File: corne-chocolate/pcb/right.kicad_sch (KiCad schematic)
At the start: 79 parts, among them J3 MJ-4PP-9, J4 Conn_01x04, P3 Conn_01x01, P4 Conn_01x01, SW13 SW_PUSH, SW22 SW_PUSH, SW23 SW_PUSH, SW24 SW_PUSH, SW25 SW_PUSH, SW26 SW_PUSH, SW27 SW_PUSH, SW28 SW_PUSH, SW29 SW_PUSH, SW30 SW_PUSH, SW31 SW_PUSH, SW32 SW_PUSH, SW33 SW_PUSH, SW34 SW_PUSH, SW35 SW_PUSH, SW36 SW_PUSH, SW37 SW_PUSH, SW7 SW_PUSH, U2 ProMicro

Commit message: several important fixes
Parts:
- removed J3: MJ-4PP-9, kbd:MJ-4PP-9_1side, symbol kbd:MJ-4PP-9
- removed J4: Conn_01x04, kbd:OLED_1side, symbol Connector_Generic:Conn_01x04
- removed JP6, JP7, JP8, JP9: Device:Jumper_NO_Small, kbd:Jumper, symbol kbd:Jumper_NO_Small-Device
- removed L13, L30, L31, L32, L33, L36, L37, L38, L39, L40, L41, L42, L43, L46, L47, L48, L49, L7: SK6812MINI, kbd:YS-SK6812MINI-E, symbol kbd:SK6812MINI
- removed L28, L29, L34, L35, L44, L45: SK6812MINI, kbd:SK6812MINI_underglow_rev, symbol kbd:SK6812MINI
- removed P3: Conn_01x01, kbd:1pin_conn, symbol Connector_Generic:Conn_01x01
- removed R3, R4: R, kbd:R, symbol Device:R
- added J3: 781271220, kbd:CON_781271220, symbol kbd:781271220
- added J4: 54-00174, kbd:54-00174_TEN, symbol kbd:54-00174
- added LED25, LED26, LED27, LED28, LED29, LED31, LED32, LED34, LED35, LED37, LED38, LED39, LED40, LED41, LED43, LED44, LED46, LED47: YS-SK6812MINI-E, kbd:LED_SK6812-MINI-E, symbol kbd:LED_SK6812MINI-E
- added LED30, LED33, LED36, LED42, LED45, LED48: WS2812B, kbd:LED_WS2812B_PLCC4_5.0x5.0mm_P3.2mm, symbol kbd:WS2812B
- added R3, R4: 4k7, kbd:R_1206_3216Metric_Pad1.30x1.75mm_HandSolder, symbol kbd:R
- D19: renamed from D7; item qty 100 -> (none); supplier Amazon -> Digikey; supplier pn B09DR5KFXM -> 1655-1N4148WCT-ND; vendor site https://www.amazon.com/Adafruit-Industries-1N4148-SOD-123-D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 -> (none)
- D20: renamed from D23; item qty 100 -> (none); supplier Amazon -> Digikey; supplier pn B09DR5KFXM -> 1655-1N4148WCT-ND; vendor site https://www.amazon.com/Adafruit-Industries-1N4148-SOD-123-D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 -> (none)
- D21: renamed from D26; item qty 100 -> (none); supplier Amazon -> Digikey; supplier pn B09DR5KFXM -> 1655-1N4148WCT-ND; vendor site https://www.amazon.com/Adafruit-Industries-1N4148-SOD-123-D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 -> (none)
- D22: renamed from D30; item qty 100 -> (none); supplier Amazon -> Digikey; supplier pn B09DR5KFXM -> 1655-1N4148WCT-ND; vendor site https://www.amazon.com/Adafruit-Industries-1N4148-SOD-123-D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 -> (none)
- D23: renamed from D34; item qty 100 -> (none); supplier Amazon -> Digikey; supplier pn B09DR5KFXM -> 1655-1N4148WCT-ND; vendor site https://www.amazon.com/Adafruit-Industries-1N4148-SOD-123-D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 -> (none)
- D24: renamed from D13; item qty 100 -> (none); supplier Amazon -> Digikey; supplier pn B09DR5KFXM -> 1655-1N4148WCT-ND; vendor site https://www.amazon.com/Adafruit-Industries-1N4148-SOD-123-D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 -> (none)
- D25: renamed from D24; item qty 100 -> (none); supplier Amazon -> Digikey; supplier pn B09DR5KFXM -> 1655-1N4148WCT-ND; vendor site https://www.amazon.com/Adafruit-Industries-1N4148-SOD-123-D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 -> (none)
- D26: renamed from D27; item qty 100 -> (none); supplier Amazon -> Digikey; supplier pn B09DR5KFXM -> 1655-1N4148WCT-ND; vendor site https://www.amazon.com/Adafruit-Industries-1N4148-SOD-123-D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 -> (none)
- D27: renamed from D31; item qty 100 -> (none); supplier Amazon -> Digikey; supplier pn B09DR5KFXM -> 1655-1N4148WCT-ND; vendor site https://www.amazon.com/Adafruit-Industries-1N4148-SOD-123-D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 -> (none)
- D28: renamed from D35; item qty 100 -> (none); supplier Amazon -> Digikey; supplier pn B09DR5KFXM -> 1655-1N4148WCT-ND; vendor site https://www.amazon.com/Adafruit-Industries-1N4148-SOD-123-D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 -> (none)
- D29: renamed from D22; item qty 100 -> (none); supplier Amazon -> Digikey; supplier pn B09DR5KFXM -> 1655-1N4148WCT-ND; vendor site https://www.amazon.com/Adafruit-Industries-1N4148-SOD-123-D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 -> (none)
- D30: renamed from D25; item qty 100 -> (none); supplier Amazon -> Digikey; supplier pn B09DR5KFXM -> 1655-1N4148WCT-ND; vendor site https://www.amazon.com/Adafruit-Industries-1N4148-SOD-123-D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 -> (none)
- D31: renamed from D28; item qty 100 -> (none); supplier Amazon -> Digikey; supplier pn B09DR5KFXM -> 1655-1N4148WCT-ND; vendor site https://www.amazon.com/Adafruit-Industries-1N4148-SOD-123-D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 -> (none)
- D32: item qty 100 -> (none); supplier Amazon -> Digikey; supplier pn B09DR5KFXM -> 1655-1N4148WCT-ND; vendor site https://www.amazon.com/Adafruit-Industries-1N4148-SOD-123-D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 -> (none)
- D33: renamed from D36; item qty 100 -> (none); supplier Amazon -> Digikey; supplier pn B09DR5KFXM -> 1655-1N4148WCT-ND; vendor site https://www.amazon.com/Adafruit-Industries-1N4148-SOD-123-D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 -> (none)
- D34: renamed from D29; item qty 100 -> (none); supplier Amazon -> Digikey; supplier pn B09DR5KFXM -> 1655-1N4148WCT-ND; vendor site https://www.amazon.com/Adafruit-Industries-1N4148-SOD-123-D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 -> (none)
- D35: renamed from D33; item qty 100 -> (none); supplier Amazon -> Digikey; supplier pn B09DR5KFXM -> 1655-1N4148WCT-ND; vendor site https://www.amazon.com/Adafruit-Industries-1N4148-SOD-123-D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 -> (none)
- D36: renamed from D37; item qty 100 -> (none); supplier Amazon -> Digikey; supplier pn B09DR5KFXM -> 1655-1N4148WCT-ND; vendor site https://www.amazon.com/Adafruit-Industries-1N4148-SOD-123-D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 -> (none)
- RSW2: item qty 50 -> (none); supplier Amazon -> Digikey; supplier 2 pn (none) -> B07H9ZSZD4; supplier pn B07H9ZSZD4 -> CKN12301-ND; supplier2 (none) -> Amazon; vendor site https://www.amazon.com/-/es/uxcell-0-118x0-236x0-197-Peque%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 -> (none)
- SW19: renamed from SW7; item qty 100 -> (none); supplier Amazon -> Digikey; supplier 2 pn (none) -> B0CPVJLMDJ; supplier pn B0CPVJLMDJ -> 1528-5118-ND; supplier2 (none) -> Amazon; vendor site https://www.amazon.com/100Pieces-Chocolate-Switches-Accesso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 -> (none)
- SW20: renamed from SW23; item qty 100 -> (none); supplier Amazon -> Digikey; supplier 2 pn (none) -> B0CPVJLMDJ; supplier pn B0CPVJLMDJ -> 1528-5118-ND; supplier2 (none) -> Amazon; vendor site https://www.amazon.com/100Pieces-Chocolate-Switches-Accesso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 -> (none)
- SW21: renamed from SW26; item qty 100 -> (none); supplier Amazon -> Digikey; supplier 2 pn (none) -> B0CPVJLMDJ; supplier pn B0CPVJLMDJ -> 1528-5118-ND; supplier2 (none) -> Amazon; vendor site https://www.amazon.com/100Pieces-Chocolate-Switches-Accesso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 -> (none)
- SW22: renamed from SW30; item qty 100 -> (none); supplier Amazon -> Digikey; supplier 2 pn (none) -> B0CPVJLMDJ; supplier pn B0CPVJLMDJ -> 1528-5118-ND; supplier2 (none) -> Amazon; vendor site https://www.amazon.com/100Pieces-Chocolate-Switches-Accesso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 -> (none)
- SW23: renamed from SW34; item qty 100 -> (none); supplier Amazon -> Digikey; supplier 2 pn (none) -> B0CPVJLMDJ; supplier pn B0CPVJLMDJ -> 1528-5118-ND; supplier2 (none) -> Amazon; vendor site https://www.amazon.com/100Pieces-Chocolate-Switches-Accesso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 -> (none)
- SW24: renamed from SW13; item qty 100 -> (none); supplier Amazon -> Digikey; supplier 2 pn (none) -> B0CPVJLMDJ; supplier pn B0CPVJLMDJ -> 1528-5118-ND; supplier2 (none) -> Amazon; vendor site https://www.amazon.com/100Pieces-Chocolate-Switches-Accesso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 -> (none)
- SW25: renamed from SW24; item qty 100 -> (none); supplier Amazon -> Digikey; supplier 2 pn (none) -> B0CPVJLMDJ; supplier pn B0CPVJLMDJ -> 1528-5118-ND; supplier2 (none) -> Amazon; vendor site https://www.amazon.com/100Pieces-Chocolate-Switches-Accesso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 -> (none)
- SW26: renamed from SW27; item qty 100 -> (none); supplier Amazon -> Digikey; supplier 2 pn (none) -> B0CPVJLMDJ; supplier pn B0CPVJLMDJ -> 1528-5118-ND; supplier2 (none) -> Amazon; vendor site https://www.amazon.com/100Pieces-Chocolate-Switches-Accesso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 -> (none)
- SW27: renamed from SW31; item qty 100 -> (none); supplier Amazon -> Digikey; supplier 2 pn (none) -> B0CPVJLMDJ; supplier pn B0CPVJLMDJ -> 1528-5118-ND; supplier2 (none) -> Amazon; vendor site https://www.amazon.com/100Pieces-Chocolate-Switches-Accesso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 -> (none)
- SW28: renamed from SW35; item qty 100 -> (none); supplier Amazon -> Digikey; supplier 2 pn (none) -> B0CPVJLMDJ; supplier pn B0CPVJLMDJ -> 1528-5118-ND; supplier2 (none) -> Amazon; vendor site https://www.amazon.com/100Pieces-Chocolate-Switches-Accesso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 -> (none)
- SW29: renamed from SW22; item qty 100 -> (none); supplier Amazon -> Digikey; supplier 2 pn (none) -> B0CPVJLMDJ; supplier pn B0CPVJLMDJ -> 1528-5118-ND; supplier2 (none) -> Amazon; vendor site https://www.amazon.com/100Pieces-Chocolate-Switches-Accesso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 -> (none)
- SW30: renamed from SW25; item qty 100 -> (none); supplier Amazon -> Digikey; supplier 2 pn (none) -> B0CPVJLMDJ; supplier pn B0CPVJLMDJ -> 1528-5118-ND; supplier2 (none) -> Amazon; vendor site https://www.amazon.com/100Pieces-Chocolate-Switches-Accesso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 -> (none)
- SW31: renamed from SW28; item qty 100 -> (none); supplier Amazon -> Digikey; supplier 2 pn (none) -> B0CPVJLMDJ; supplier pn B0CPVJLMDJ -> 1528-5118-ND; supplier2 (none) -> Amazon; vendor site https://www.amazon.com/100Pieces-Chocolate-Switches-Accesso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 -> (none)
- SW32: item qty 100 -> (none); supplier Amazon -> Digikey; supplier 2 pn (none) -> B0CPVJLMDJ; supplier pn B0CPVJLMDJ -> 1528-5118-ND; supplier2 (none) -> Amazon; vendor site https://www.amazon.com/100Pieces-Chocolate-Switches-Accesso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 -> (none)
- SW33: renamed from SW36; item qty 100 -> (none); supplier Amazon -> Digikey; supplier 2 pn (none) -> B0CPVJLMDJ; supplier pn B0CPVJLMDJ -> 1528-5118-ND; supplier2 (none) -> Amazon; vendor site https://www.amazon.com/100Pieces-Chocolate-Switches-Accesso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 -> (none)
- SW34: renamed from SW29; item qty 100 -> (none); supplier Amazon -> Digikey; supplier 2 pn (none) -> B0CPVJLMDJ; supplier pn B0CPVJLMDJ -> 1528-5118-ND; supplier2 (none) -> Amazon; vendor site https://www.amazon.com/100Pieces-Chocolate-Switches-Accesso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 -> (none)
- SW35: renamed from SW33; item qty 100 -> (none); supplier Amazon -> Digikey; supplier 2 pn (none) -> B0CPVJLMDJ; supplier pn B0CPVJLMDJ -> 1528-5118-ND; supplier2 (none) -> Amazon; vendor site https://www.amazon.com/100Pieces-Chocolate-Switches-Accesso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 -> (none)
- SW36: renamed from SW37; item qty 100 -> (none); supplier Amazon -> Digikey; supplier 2 pn (none) -> B0CPVJLMDJ; supplier pn B0CPVJLMDJ -> 1528-5118-ND; supplier2 (none) -> Amazon; vendor site https://www.amazon.com/100Pieces-Chocolate-Switches-Accesso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 -> (none)
- U2: supplier (none) -> Digikey; supplier 2 pn (none) -> B09TKMM8N5; supplier pn (none) -> 1568-1060-ND; supplier2 (none) -> Amazon
- renumbered H11 to H10, H13 to H11, H14 to H12, H9 to H13, H8 to H14, H10 to H8, H12 to H9, P4 to P2
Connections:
- net RGND: now also J3.2, J4.1, LED25.3 (VSS), LED26.3 (VSS), LED27.3 (VSS), LED28.3 (VSS), LED29.3 (VSS), LED30.3 (VSS), LED31.3 (VSS), LED32.3 (VSS), LED33.3 (VSS), LED34.3 (VSS), LED35.3 (VSS), LED36.3 (VSS), LED37.3 (VSS), LED38.3 (VSS), LED39.3 (VSS), LED40.3 (VSS), LED41.3 (VSS), LED42.3 (VSS), LED43.3 (VSS), LED44.3 (VSS), LED45.3 (VSS), LED46.3 (VSS), LED47.3 (VSS), LED48.3 (VSS)
- net RLED: now also LED25.4 (DIN)
- net RSCL: now also J3.4, R4.2
- net RSDA: now also J3.3, R3.2
- net RVCC: now also J3.1, J4.2, LED25.1 (VDD), LED26.1 (VDD), LED27.1 (VDD), LED28.1 (VDD), LED29.1 (VDD), LED30.1 (VDD), LED31.1 (VDD), LED32.1 (VDD), LED33.1 (VDD), LED34.1 (VDD), LED35.1 (VDD), LED36.1 (VDD), LED37.1 (VDD), LED38.1 (VDD), LED39.1 (VDD), LED40.1 (VDD), LED41.1 (VDD), LED42.1 (VDD), LED43.1 (VDD), LED44.1 (VDD), LED45.1 (VDD), LED46.1 (VDD), LED47.1 (VDD), LED48.1 (VDD), R3.1, R4.1
- net Rdata: now also J4.4
- new net: LED31.4 (DIN), LED32.2 (DOUT)
- new net: LED32.4 (DIN), LED33.2 (DOUT)
- new net: LED26.2 (DOUT), LED27.4 (DIN)
- new net: LED25.2 (DOUT), LED26.4 (DIN)
- new net: LED43.2 (DOUT), LED48.4 (DIN)
- new net: LED42.2 (DOUT), LED43.4 (DIN)
- new net: LED44.4 (DIN), LED45.2 (DOUT)
- new net: LED47.4 (DIN), LED48.2 (DOUT)
- new net: LED33.4 (DIN), LED34.2 (DOUT)
- new net: LED41.2 (DOUT), LED42.4 (DIN)
- new net: LED40.2 (DOUT), LED41.4 (DIN)
- new net: LED39.2 (DOUT), LED40.4 (DIN)
- new net: LED38.2 (DOUT), LED39.4 (DIN)
- new net: LED36.4 (DIN), LED37.2 (DOUT)
- new net: LED29.2 (DOUT), LED37.4 (DIN)
- new net: LED27.2 (DOUT), LED28.4 (DIN)
- new net: LED35.4 (DIN), LED36.2 (DOUT)
- new net: LED34.4 (DIN), LED35.2 (DOUT)
- new net: LED28.2 (DOUT), LED29.4 (DIN)
- new net: LED45.4 (DIN), LED46.2 (DOUT)
- new net: LED46.4 (DIN), LED47.2 (DOUT)
- new net: LED30.2 (DOUT), LED38.4 (DIN)
- new net: LED30.4 (DIN), LED31.2 (DOUT)
- no-connect marks 7 -> 17
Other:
- moved on the sheet: P2

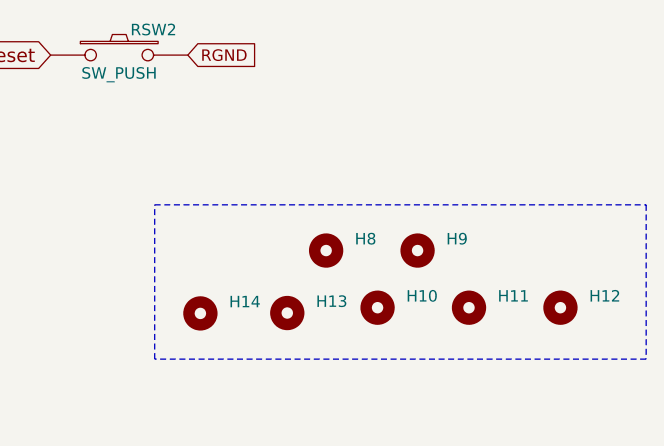
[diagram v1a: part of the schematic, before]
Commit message: breakaway tabs
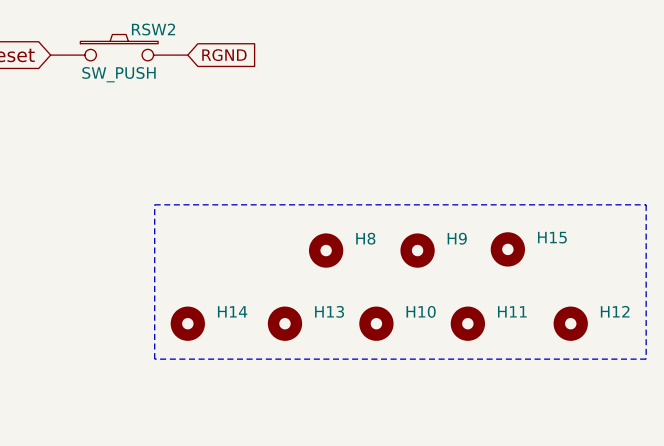
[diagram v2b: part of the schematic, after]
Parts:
- added H15: MountingHole, MountingHole:MountingHole_2.2mm_M2_ISO14580, symbol Mechanical:MountingHole
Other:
- moved on the sheet: H10, H11, H12, H13, H14

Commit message: zones in right keyboard
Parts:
- H10, H11, H12, H13, H14: footprint MountingHole:MountingHole_4.3mm_M4_ISO14580 -> MountingHole:MountingHole_2.2mm_M2_ISO14580
- J3: supplier (none) -> Digikey; supplier pn (none) -> 900-0781271220CT-ND
- R3, R4: footprint kbd:R_1206_3216Metric_Pad1.30x1.75mm_HandSolder -> kbd:R_0805_2012Metric_Pad1.20x1.40mm_HandSolder
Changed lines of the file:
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@@
       (effects (font (size 1.27 1.27) italic) hide)
+    )
+    (property "supplier" "Digikey" (at 170.815 102.87 0)
+      (effects (font (size 1.27 1.27)) hide)
+    )
+    (property "supplier pn" "900-0781271220CT-ND" (at 170.815 102.87 0)
+      (effects (font (size 1.27 1.27)) hide)
     )
     (pin "9")
@@
       (effects (font (size 1.27 1.27)) (justify left) hide)
     )
-    (property "Footprint" "MountingHole:MountingHole_4.3mm_M4_ISO14580" (at 268.605 158.75 0)
+    (property "Footprint" "MountingHole:MountingHole_2.2mm_M2_ISO14580" (at 268.605 158.75 0)
       (effects (font (size 1.27 1.27)) hide)
     )
@@
       (effects (font (size 1.27 1.27)) (justify left) hide)
     )
-    (property "Footprint" "MountingHole:MountingHole_4.3mm_M4_ISO14580" (at 236.855 158.75 0)
+    (property "Footprint" "MountingHole:MountingHole_2.2mm_M2_ISO14580" (at 236.855 158.75 0)
       (effects (font (size 1.27 1.27)) hide)
     )
@@
       (effects (font (size 1.27 1.27)) (justify left))
     )
-    (property "Footprint" "kbd:R_1206_3216Metric_Pad1.30x1.75mm_HandSolder" (at 110.617 55.245 90)
+    (property "Footprint" "kbd:R_0805_2012Metric_Pad1.20x1.40mm_HandSolder" (at 110.617 55.245 90)
       (effects (font (size 1.27 1.27)) hide)
     )
@@
       (effects (font (size 1.27 1.27)) (justify left) hide)
     )
-    (property "Footprint" "MountingHole:MountingHole_4.3mm_M4_ISO14580" (at 257.175 158.75 0)
+    (property "Footprint" "MountingHole:MountingHole_2.2mm_M2_ISO14580" (at 257.175 158.75 0)
       (effects (font (size 1.27 1.27)) hide)
     )
@@
       (effects (font (size 1.27 1.27)) (justify left) hide)
     )
-    (property "Footprint" "MountingHole:MountingHole_4.3mm_M4_ISO14580" (at 247.015 158.75 0)
+    (property "Footprint" "MountingHole:MountingHole_2.2mm_M2_ISO14580" (at 247.015 158.75 0)
       (effects (font (size 1.27 1.27)) hide)
     )
@@
     )
   )
-  (symbol (lib_name "R_1") (lib_id "kbd:R") (at 104.775 55.245 0) (unit 1)
+  (symbol (lib_id "kbd:R") (at 104.775 55.245 0) (unit 1)
     (in_bom yes) (on_board yes) (dnp no)
     (property "Reference" "R3" (at 106.68 53.975 0)
@@
       (effects (font (size 1.27 1.27)) (justify left))
     )
-    (property "Footprint" "kbd:R_1206_3216Metric_Pad1.30x1.75mm_HandSolder" (at 102.997 55.245 90)
+    (property "Footprint" "kbd:R_0805_2012Metric_Pad1.20x1.40mm_HandSolder" (at 102.997 55.245 90)
       (effects (font (size 1.27 1.27)) hide)
     )
@@
       (effects (font (size 1.27 1.27)) (justify left) hide)
     )
-    (property "Footprint" "MountingHole:MountingHole_4.3mm_M4_ISO14580" (at 226.06 158.75 0)
-      (effects (font (size 1.27 1.27)) hide)
-    )
+    (property "Footprint" "MountingHole:MountingHole_2.2mm_M2_ISO14580" (at 226.06 158.75 0)
+      (effects (font (size 1.27 1.27)) hide)
+    )

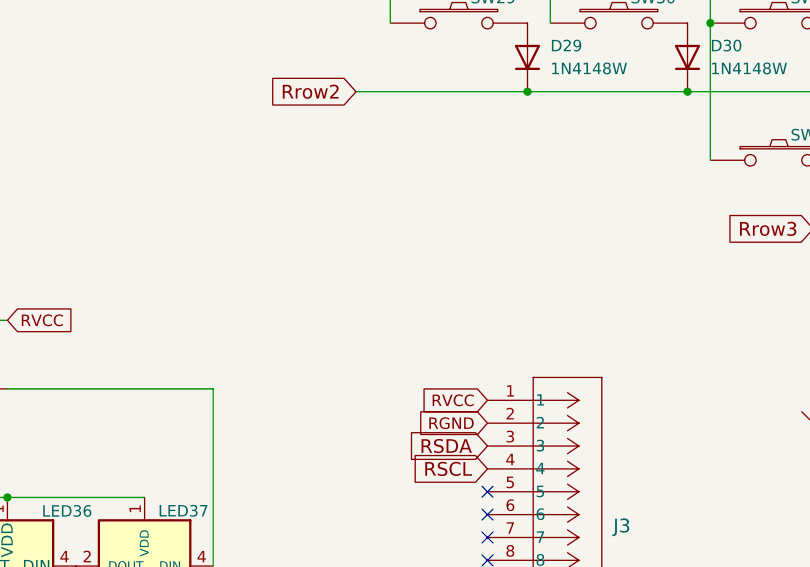
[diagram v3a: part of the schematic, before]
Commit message: zones in left keyboard
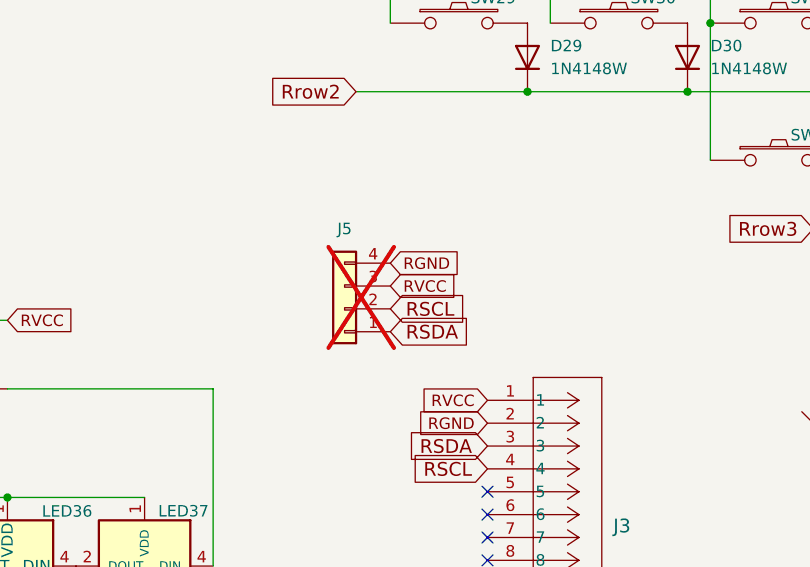
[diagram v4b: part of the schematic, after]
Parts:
- added J5: Conn_01x04, kbd:OLED_1side, symbol Connector_Generic:Conn_01x04
- R3, R4: supplier pn 311-4.70KFRCT-ND -> 311-4.70KCRCT-ND
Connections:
- net RGND: now also J5.4 (Pin_4)
- net RSCL: now also J5.2 (Pin_2)
- net RSDA: now also J5.1 (Pin_1)
- net RVCC: now also J5.3 (Pin_3)
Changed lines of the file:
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@@
     (fill (type none))
+  )
+  (global_label "RSCL" (shape input) (at 160.02 92.71 0) (fields_autoplaced)
+    (effects (font (size 1.524 1.524)) (justify left))
+    (property "Intersheetrefs" "${INTERSHEET_REFS}" (at 168.5499 92.71 0)
+      (effects (font (size 1.27 1.27)) (justify left) hide)
+    )
   )
   (global_label "Rdata" (shape input) (at 46.99 44.45 180) (fields_autoplaced)
@@
     )
   )
+  (global_label "RSDA" (shape input) (at 160.02 95.25 0) (fields_autoplaced)
+    (effects (font (size 1.524 1.524)) (justify left))
+    (property "Intersheetrefs" "${INTERSHEET_REFS}" (at 168.6225 95.25 0)
+      (effects (font (size 1.27 1.27)) (justify left) hide)
+    )
+  )
   (global_label "RVCC" (shape input) (at 117.475 93.98 0) (fields_autoplaced)
     (effects (font (size 1.27 1.27)) (justify left))
@@
     )
   )
+  (global_label "RVCC" (shape input) (at 160.02 90.17 0) (fields_autoplaced)
+    (effects (font (size 1.27 1.27)) (justify left))
+    (property "Intersheetrefs" "${INTERSHEET_REFS}" (at 167.2496 90.17 0)
+      (effects (font (size 1.27 1.27)) (justify left) hide)
+    )
+  )
   (global_label "Rrow1" (shape input) (at 46.99 59.69 180) (fields_autoplaced)
     (effects (font (size 1.1938 1.1938)) (justify right))
@@
     (effects (font (size 1.524 1.524)) (justify left))
     (property "Intersheetrefs" "${INTERSHEET_REFS}" (at 249.3584 109.22 0)
+      (effects (font (size 1.27 1.27)) (justify left) hide)
+    )
+  )
+  (global_label "RGND" (shape input) (at 160.02 87.63 0) (fields_autoplaced)
+    (effects (font (size 1.27 1.27)) (justify left))
+    (property "Intersheetrefs" "${INTERSHEET_REFS}" (at 167.4915 87.63 0)
       (effects (font (size 1.27 1.27)) (justify left) hide)
     )
@@
       (effects (font (size 1.27 1.27)) hide)
     )
-    (property "Datasheet" "~" (at 112.395 55.245 0)
+    (property "Datasheet" "https://www.yageo.com/upload/media/product/products/datasheet/rchip/PYu-RC_Group_51_RoHS_L_12.pdf" (at 112.395 55.245 0)
       (effects (font (size 1.27 1.27)) hide)
     )
@@
       (effects (font (size 1.27 1.27)) hide)
     )
-    (property "supplier pn" "311-4.70KFRCT-ND" (at 112.395 55.245 0)
+    (property "supplier pn" "311-4.70KCRCT-ND" (at 112.395 55.245 0)
       (effects (font (size 1.27 1.27)) hide)
     )
@@
         (path "/b2404ab0-025a-473e-9fbb-0abc932972cf/29bacd27-a657-4ec1-852c-714ea039bec7"
           (reference "R4") (unit 1)
+        )
+      )
+    )
+  )
+  (symbol (lib_id "Connector_Generic:Conn_01x04") (at 154.94 92.71 180) (unit 1)
+    (in_bom yes) (on_board yes) (dnp yes)
+    (property "Reference" "J5" (at 154.94 83.82 0)
+      (effects (font (size 1.27 1.27)))
+    )
+    (property "Value" "Conn_01x04" (at 154.94 85.09 0)
+      (effects (font (size 1.27 1.27)) hide)
+    )
+    (property "Footprint" "kbd:OLED_1side" (at 154.94 92.71 0)
+      (effects (font (size 1.27 1.27)) hide)
+    )
+    (property "Datasheet" "https://robu.in/wp-content/uploads/2019/12/ER-OLEDM0.91-1_Datasheet_617717.pdf" (at 154.94 92.71 0)
+      (effects (font (size 1.27 1.27)) hide)
+    )
+    (property "supplier" "Amazon" (at 154.94 92.71 0)
+      (effects (font (size 1.27 1.27)) hide)
+    )
+    (property "supplier pn" "B0925V1DZK" (at 154.94 92.71 0)
+      (effects (font (size 1.27 1.27)) hide)
+    )
+    (property "fp check" "Y" (at 154.94 92.71 0)
+      (effects (font (size 1.27 1.27)) hide)
+    )
+    (property "supplier 2 pn" "" (at 154.94 92.71 0)
+      (effects (font (size 1.27 1.27)) hide)
+    )
+    (property "supplier2" "" (at 154.94 92.71 0)
+      (effects (font (size 1.27 1.27)) hide)
+    )
+    (pin "1")
+    (pin "2")
+    (pin "3")
+    (pin "4")
+    (instances
+      (project "corne-chocolate"
+        (path "/b2404ab0-025a-473e-9fbb-0abc932972cf/29bacd27-a657-4ec1-852c-714ea039bec7"
+          (reference "J5") (unit 1)
         )
       )
@@
       (effects (font (size 1.27 1.27)) hide)
     )
-    (property "Datasheet" "~" (at 104.775 55.245 0)
+    (property "Datasheet" "https://www.yageo.com/upload/media/product/products/datasheet/rchip/PYu-RC_Group_51_RoHS_L_12.pdf" (at 104.775 55.245 0)
       (effects (font (size 1.27 1.27)) hide)
     )
@@
       (effects (font (size 1.27 1.27)) hide)
     )
-    (property "supplier pn" "311-4.70KFRCT-ND" (at 104.775 55.245 0)
-      (effects (font (size 1.27 1.27)) hide)
-    )
+    (property "supplier pn" "311-4.70KCRCT-ND" (at 104.775 55.245 0)
+      (effects (font (size 1.27 1.27)) hide)
+    )
